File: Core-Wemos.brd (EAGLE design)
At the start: 86.5 x 100 mm, 48 parts, among them J2 CONNECTOR-GROVE-4P-2.0-347013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

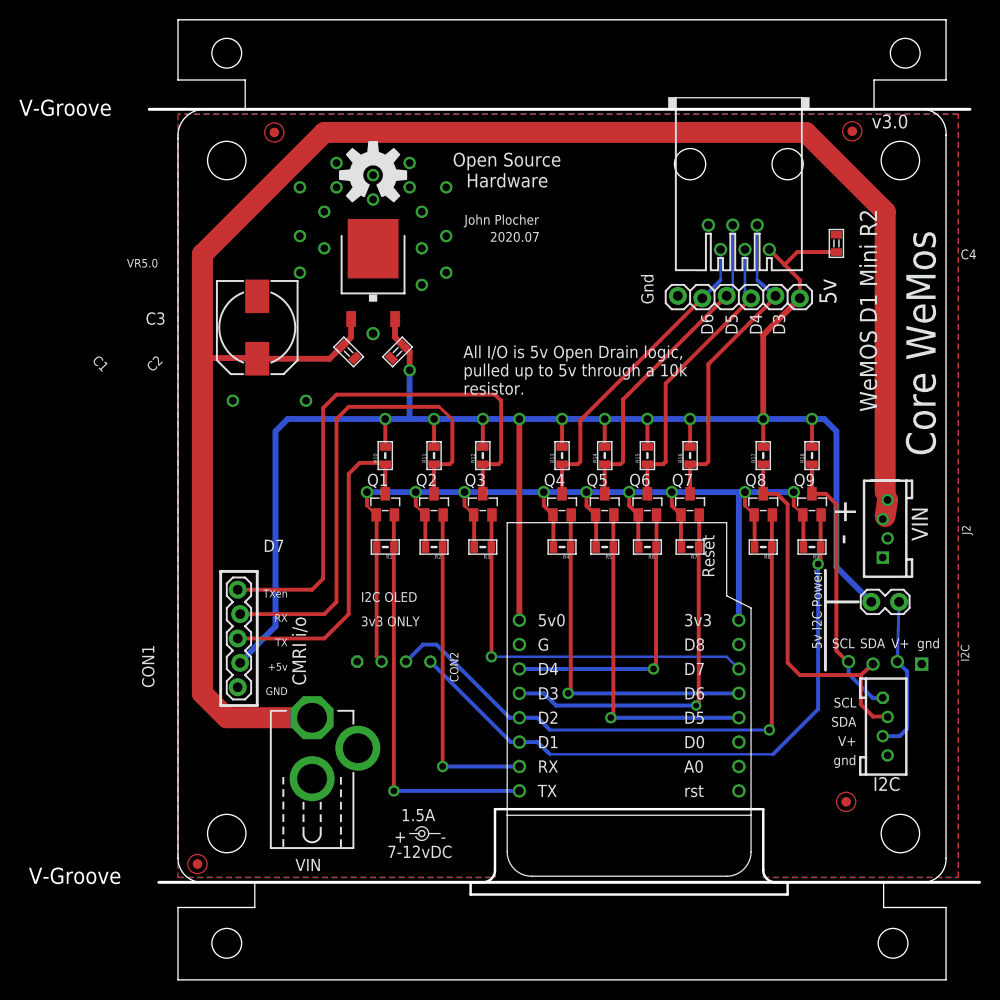
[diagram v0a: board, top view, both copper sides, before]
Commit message: realigned I2C connectors, added power on LED
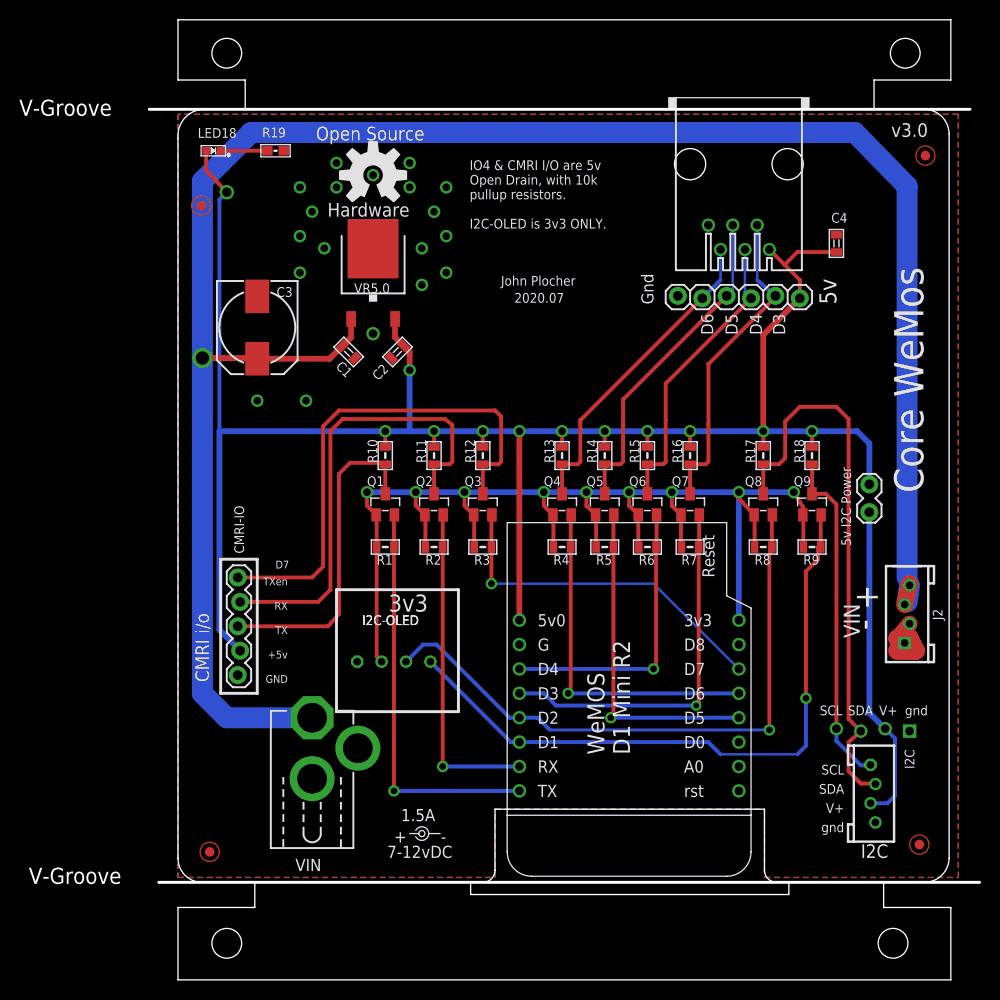
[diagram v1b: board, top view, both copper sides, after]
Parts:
- removed CON1: (no value), SPCoast:CON-CMRI-IO
- added CMRI-IO: (no value), SPCoast:CON-CMRI-IO
- added LED18: G, SPCoast:0603-LED
- added R19: 2K0, SPCoast:0603-RES
- BOARD: device SPCoast:BOARD-DINRAIL-3.17INX8CM -> SPCoast:BOARD-DINRAIL-3.17INX8CM-NOHOLES
- J3: value (none) -> IO4
- moved FID3 10.8 mm to (2.41, 70.5)
- moved JP1 9.96 mm to (72.0, 38.7), turned to 90 degrees
- moved J2 9.18 mm to (75.9, 27.9)
- moved FID1 8.82 mm to (77.2, 3.94)
- moved FID4 8.03 mm to (77.9, 75.7)
- moved I2C 7.10 mm to (72.4, 15.9)
- moved FID2 1.80 mm to (3.30, 3.17)
- renumbered CON2 to I2C-OLED
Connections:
- new net GND1: R19.2
- new net N$1: LED18.C, R19.1
- net D7H: now also CMRI-IO.5; no longer CON1.5
- net GND: now also CMRI-IO.1; no longer CON1.1
- net RXH: now also CMRI-IO.4; no longer CON1.4
- net TXH: now also CMRI-IO.3; no longer CON1.3
- net VCCIO: now also CMRI-IO.2, LED18.A; no longer CON1.2
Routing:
- net SDAH: track 38.8 -> 58.3 mm
- net +9V: track 188.6 -> 208.0 mm, vias 0 -> 1
- net N$44: track 16.5 -> 33.5 mm
- net VCCIO: track 192.4 -> 202.0 mm, vias 11 -> 12
- net GND: track 0.00 -> 6.59 mm, vias 20 -> 19
- net SCLH: track 29.0 -> 35.5 mm
- net N$1: track 0.00 -> 4.88 mm
- net D7H: track 58.0 -> 53.3 mm
- net D7: track 41.1 -> 36.6 mm
- net RXH: track 52.2 -> 48.8 mm
- net SCL: track 66.7 -> 68.3 mm
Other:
- outline, holes or cut-outs redrawn
- board text added: "3v3"
- board text added: "IO4 & CMRI I/O are 5v Open Drain, with 10k pullup resistors. I2C-OLED is 3v3 ONLY."
- board text removed: "3v3 ONLY"
- board text removed: "All I/O is 5v Open Drain logic, pulled up to 5v through a 10k resistor."

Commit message: Silkscreen 4.0 change
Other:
- board text added: "v4.0"
- board text removed: "v3.0"
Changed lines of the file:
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@@
 <grid distance="50" unitdist="mil" unit="mil" style="dots" multiple="2" display="yes" altdistance="5" altunitdist="mil" altunit="mil"/>
 <layers>
-<layer number="1" name="Top" color="4" fill="1" visible="no" active="yes"/>
-<layer number="16" name="Bottom" color="2" fill="1" visible="no" active="yes"/>
+<layer number="1" name="Top" color="4" fill="1" visible="yes" active="yes"/>
+<layer number="16" name="Bottom" color="2" fill="1" visible="yes" active="yes"/>
 <layer number="17" name="Pads" color="23" fill="1" visible="yes" active="yes"/>
 <layer number="18" name="Vias" color="29" fill="1" visible="yes" active="yes"/>
-<layer number="19" name="Unrouted" color="6" fill="1" visible="no" active="yes"/>
+<layer number="19" name="Unrouted" color="6" fill="1" visible="yes" active="yes"/>
 <layer number="20" name="Dimension" color="15" fill="1" visible="yes" active="yes"/>
 <layer number="21" name="tPlace" color="19" fill="1" visible="yes" active="yes"/>
 <layer number="22" name="bPlace" color="17" fill="1" visible="no" active="yes"/>
-<layer number="23" name="tOrigins" color="30" fill="1" visible="no" active="yes"/>
+<layer number="23" name="tOrigins" color="30" fill="1" visible="yes" active="yes"/>
 <layer number="24" name="bOrigins" color="15" fill="1" visible="no" active="yes"/>
-<layer number="25" name="tNames" color="63" fill="1" visible="no" active="yes"/>
+<layer number="25" name="tNames" color="63" fill="1" visible="yes" active="yes"/>
 <layer number="26" name="bNames" color="34" fill="1" visible="no" active="yes"/>
 <layer number="27" name="tValues" color="56" fill="1" visible="yes" active="yes"/>
@@
 <layer number="42" name="bRestrict" color="3" fill="10" visible="no" active="yes"/>
 <layer number="43" name="vRestrict" color="2" fill="10" visible="no" active="yes"/>
-<layer number="44" name="Drills" color="16" fill="1" visible="no" active="yes"/>
-<layer number="45" name="Holes" color="35" fill="1" visible="no" active="yes"/>
-<layer number="46" name="Milling" color="50" fill="1" visible="no" active="yes"/>
-<layer number="47" name="Measures" color="21" fill="1" visible="no" active="yes"/>
+<layer number="44" name="Drills" color="16" fill="1" visible="yes" active="yes"/>
+<layer number="45" name="Holes" color="35" fill="1" visible="yes" active="yes"/>
+<layer number="46" name="Milling" color="50" fill="1" visible="yes" active="yes"/>
+<layer number="47" name="Measures" color="21" fill="1" visible="yes" active="yes"/>
 <layer number="48" name="Document" color="24" fill="1" visible="yes" active="yes"/>
-<layer number="49" name="Reference" color="48" fill="1" visible="no" active="yes"/>
+<layer number="49" name="Reference" color="48" fill="1" visible="yes" active="yes"/>
 <layer number="50" name="dxf" color="7" fill="1" visible="no" active="yes"/>
 <layer number="51" name="tDocu" color="24" fill="1" visible="yes" active="yes"/>
@@
 <text x="58.293" y="57.023" size="1.27" layer="21" rot="R90">D5</text>
 <text x="55.753" y="57.023" size="1.27" layer="21" rot="R90">D6</text>
-<text x="74.28024375" y="77.642259375" size="1.4224" layer="21">v3.0</text>
+<text x="74.28024375" y="77.642259375" size="1.4224" layer="21">v4.0</text>
 <text x="3.228040625" y="20.85159375" size="1.4224" layer="21" ratio="10" rot="R90">CMRI i/o</text>
 <text x="10.16" y="32.6898" size="0.8128" layer="21">D7</text>
@@
 <wire x1="29.21" y1="17.78" x2="29.21" y2="30.48" width="0.3048" layer="21"/>
 <wire x1="29.21" y1="30.48" x2="16.51" y2="30.48" width="0.3048" layer="21"/>
+<text x="11.35235625" y="84.920028125" size="3.048" layer="21" ratio="15" rot="SR0">Core WeMos</text>
+<text x="41.26024375" y="86.532259375" size="1.4224" layer="21">v4.0</text>
+<text x="41.38724375" y="84.500759375" size="1.016" layer="21">2020.07</text>
 </plain>
 <attributes>
